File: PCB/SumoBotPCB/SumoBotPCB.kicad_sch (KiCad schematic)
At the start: 23 parts, among them M1 Motor_DC, M2 Motor_DC, M3 Motor_DC, M4 Motor_DC, SW1 SW_Push, U1 TB6612FNG, U10 VL53L0X-GY530, U11 VL53L0X-GY530, U12 VL53L0X-GY530, U2 hc-05_BLUETOOTH_MODULE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

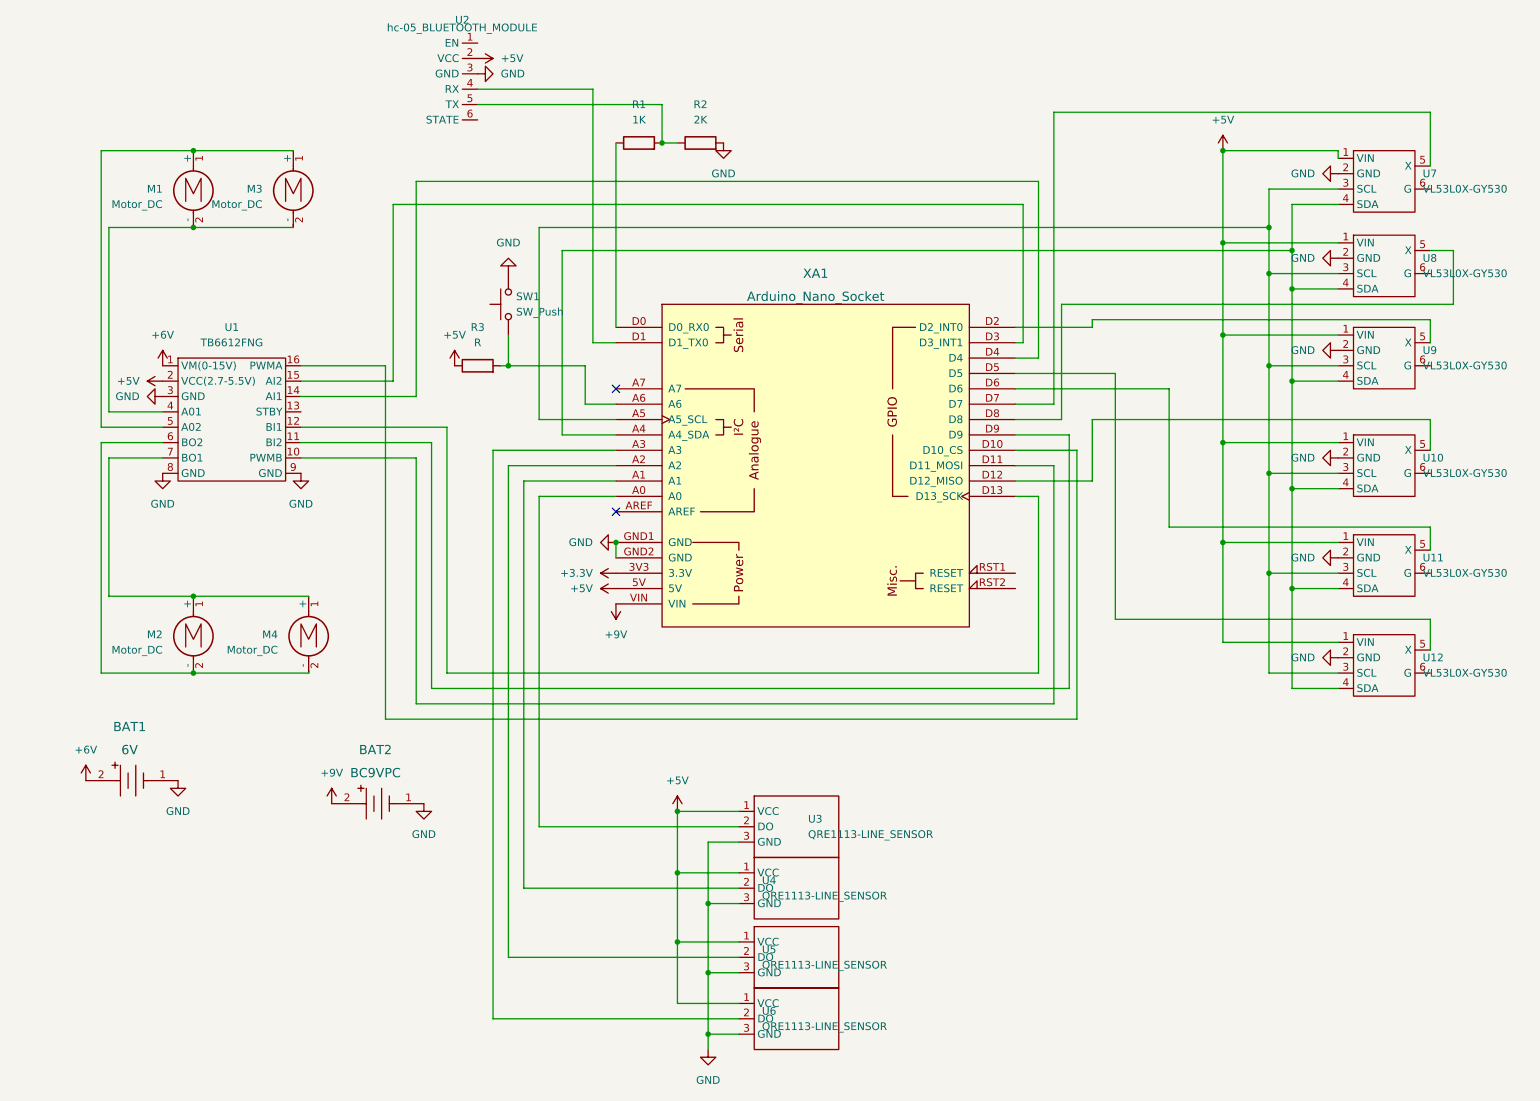
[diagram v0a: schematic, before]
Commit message: motor driver pwm
correct pin assignment to have motor driver use 6 pwm pins to allow all options.
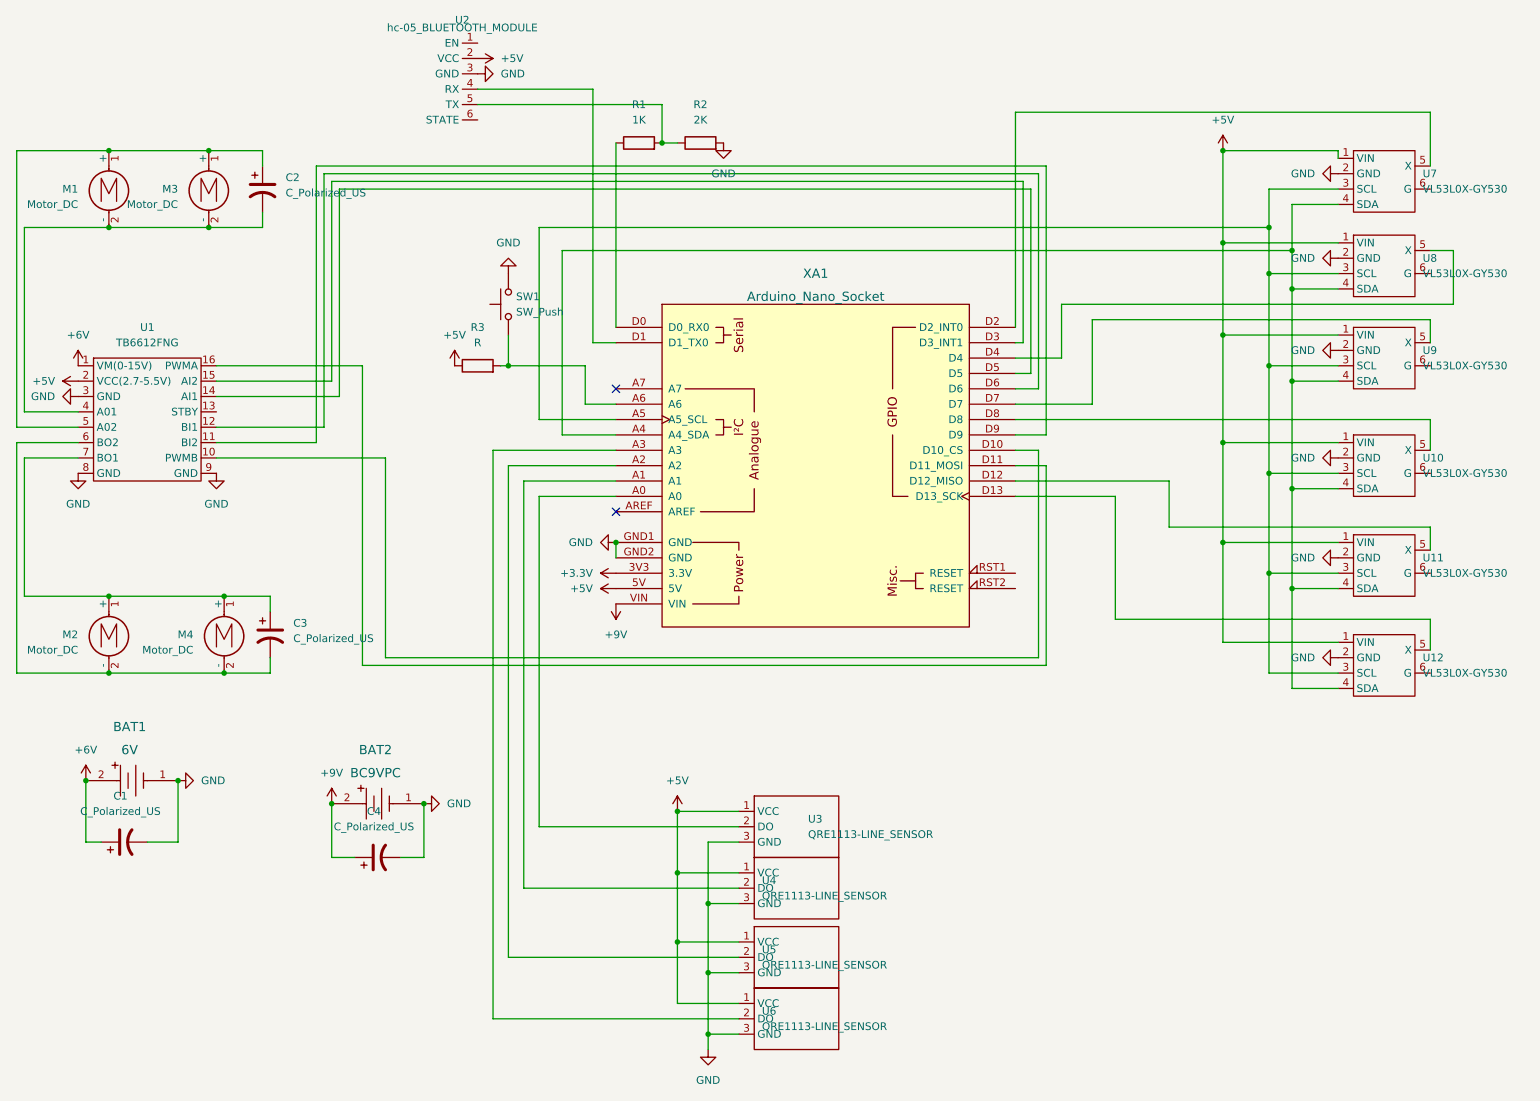
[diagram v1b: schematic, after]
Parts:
- added C1, C2, C3, C4: C_Polarized_US, Capacitor_THT:CP_Radial_D8.0mm_P5.00mm, symbol Device:C_Polarized_US
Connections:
- net +6V: now also C1.1
- net +9V: now also C4.1
- net GND: now also C1.2, C4.2
- net at M1.1 (+), M3.1 (+), U1.5 (A02): now also C2.1
- net at M1.2 (-), M3.2 (-), U1.4 (A01): now also C2.2
- net at U7.5 (X): now also XA1.D2 (D2_INT0); no longer XA1.D7
- net at M2.1 (+), M4.1 (+), U1.7 (BO1): now also C3.1
- net at M2.2 (-), M4.2 (-), U1.6 (BO2): now also C3.2
- net at U12.5 (X): now also XA1.D13 (D13_SCK); no longer XA1.D5
- net at U8.5 (X): now also XA1.D4; no longer XA1.D8
- net at U9.5 (X): now also XA1.D7; no longer XA1.D2 (D2_INT0)
- net at XA1.D10 (D10_CS): now also U1.10 (PWMB); no longer U1.16 (PWMA)
- net at XA1.D11 (D11_MOSI): now also U1.16 (PWMA); no longer U1.10 (PWMB)
- net at XA1.D12 (D12_MISO): now also U11.5 (X); no longer U10.5 (X)
- net at U1.12 (BI1): now also XA1.D6; no longer XA1.D13 (D13_SCK)
- net at U1.14 (AI1): now also XA1.D5; no longer XA1.D4
- new net: U10.5 (X), XA1.D8
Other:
- moved on the sheet: M1, M2, M3, M4, U1

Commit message: ADDED STANDBY SWITCH
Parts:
- added SW2: SW_SPDT, custom:SpDt SlideSwitch, symbol Switch:SW_SPDT
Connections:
- net +5V: now also SW2.1 (A)
- net at U1.13 (STBY): now also SW2.2 (B)
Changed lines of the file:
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@@
+    (stroke (width 0) (type default) (color 0 0 0 0))
+  )
+  (wire (pts (xy 54.61 64.77) (xy 54.61 53.34))
     (stroke (width 0) (type default) (color 0 0 0 0))
   )
@@
   )
   (wire (pts (xy 30.48 107.95) (xy 15.24 107.95))
+    (stroke (width 0) (type default) (color 0 0 0 0))
+  )
+  (wire (pts (xy 48.26 64.77) (xy 54.61 64.77))
     (stroke (width 0) (type default) (color 0 0 0 0))
   )
@@
     )
     (property "Datasheet" "" (id 3) (at 25.4 57.15 0)
+      (effects (font (size 1.27 1.27)) hide)
+    )
+    (pin "1")
+  )
+  (symbol (lib_id "power:+5V") (at 52.07 43.18 0) (unit 1)
+    (in_bom yes) (on_board yes) (fields_autoplaced)
+    (property "Reference" "#PWR0128" (id 0) (at 52.07 46.99 0)
+      (effects (font (size 1.27 1.27)) hide)
+    )
+    (property "Value" "+5V" (id 1) (at 52.07 38.1 0))
+    (property "Footprint" "" (id 2) (at 52.07 43.18 0)
+      (effects (font (size 1.27 1.27)) hide)
+    )
+    (property "Datasheet" "" (id 3) (at 52.07 43.18 0)
       (effects (font (size 1.27 1.27)) hide)
     )
@@
     (pin "1")
   )
+  (symbol (lib_id "Switch:SW_SPDT") (at 54.61 48.26 90) (unit 1)
+    (in_bom yes) (on_board yes) (fields_autoplaced)
+    (property "Reference" "SW2" (id 0) (at 58.42 46.9899 90)
+      (effects (font (size 1.27 1.27)) (justify right))
+    )
+    (property "Value" "SW_SPDT" (id 1) (at 58.42 49.5299 90)
+      (effects (font (size 1.27 1.27)) (justify right))
+    )
+    (property "Footprint" "custom:SpDt SlideSwitch" (id 2) (at 54.61 48.26 0)
+      (effects (font (size 1.27 1.27)) hide)
+    )
+    (property "Datasheet" "~" (id 3) (at 54.61 48.26 0)
+      (effects (font (size 1.27 1.27)) hide)
+    )
+    (pin "1")
+    (pin "2")
+    (pin "3")
+  )
   (symbol (lib_id "Switch:SW_Push") (at 96.52 46.99 90) (unit 1)
     (in_bom yes) (on_board yes) (fields_autoplaced)
@@
       (reference "#PWR0127") (unit 1) (value "GND") (footprint "")
     )
+    (path "/58827ba0-4d07-44f4-b07b-8842098ca099"
+      (reference "#PWR0128") (unit 1) (value "+5V") (footprint "")
+    )
     (path "/c13e6644-1617-41c6-92ae-d1ca64618352"
       (reference "BAT1") (unit 1) (value "6V") (footprint "Connector_PinHeader_2.54mm:PinHeader_1x02_P2.54mm_Vertical")
@@
       (reference "SW1") (unit 1) (value "SW_Push") (footprint "Button_Switch_THT:SW_PUSH_6mm_H4.3mm")
     )
+    (path "/b01b6e50-2c09-4c1a-87df-69dce96dfaa6"
+      (reference "SW2") (unit 1) (value "SW_SPDT") (footprint "custom:SpDt SlideSwitch")
+    )
     (path "/f86527b4-a225-4f07-a789-d53d38094b3b"

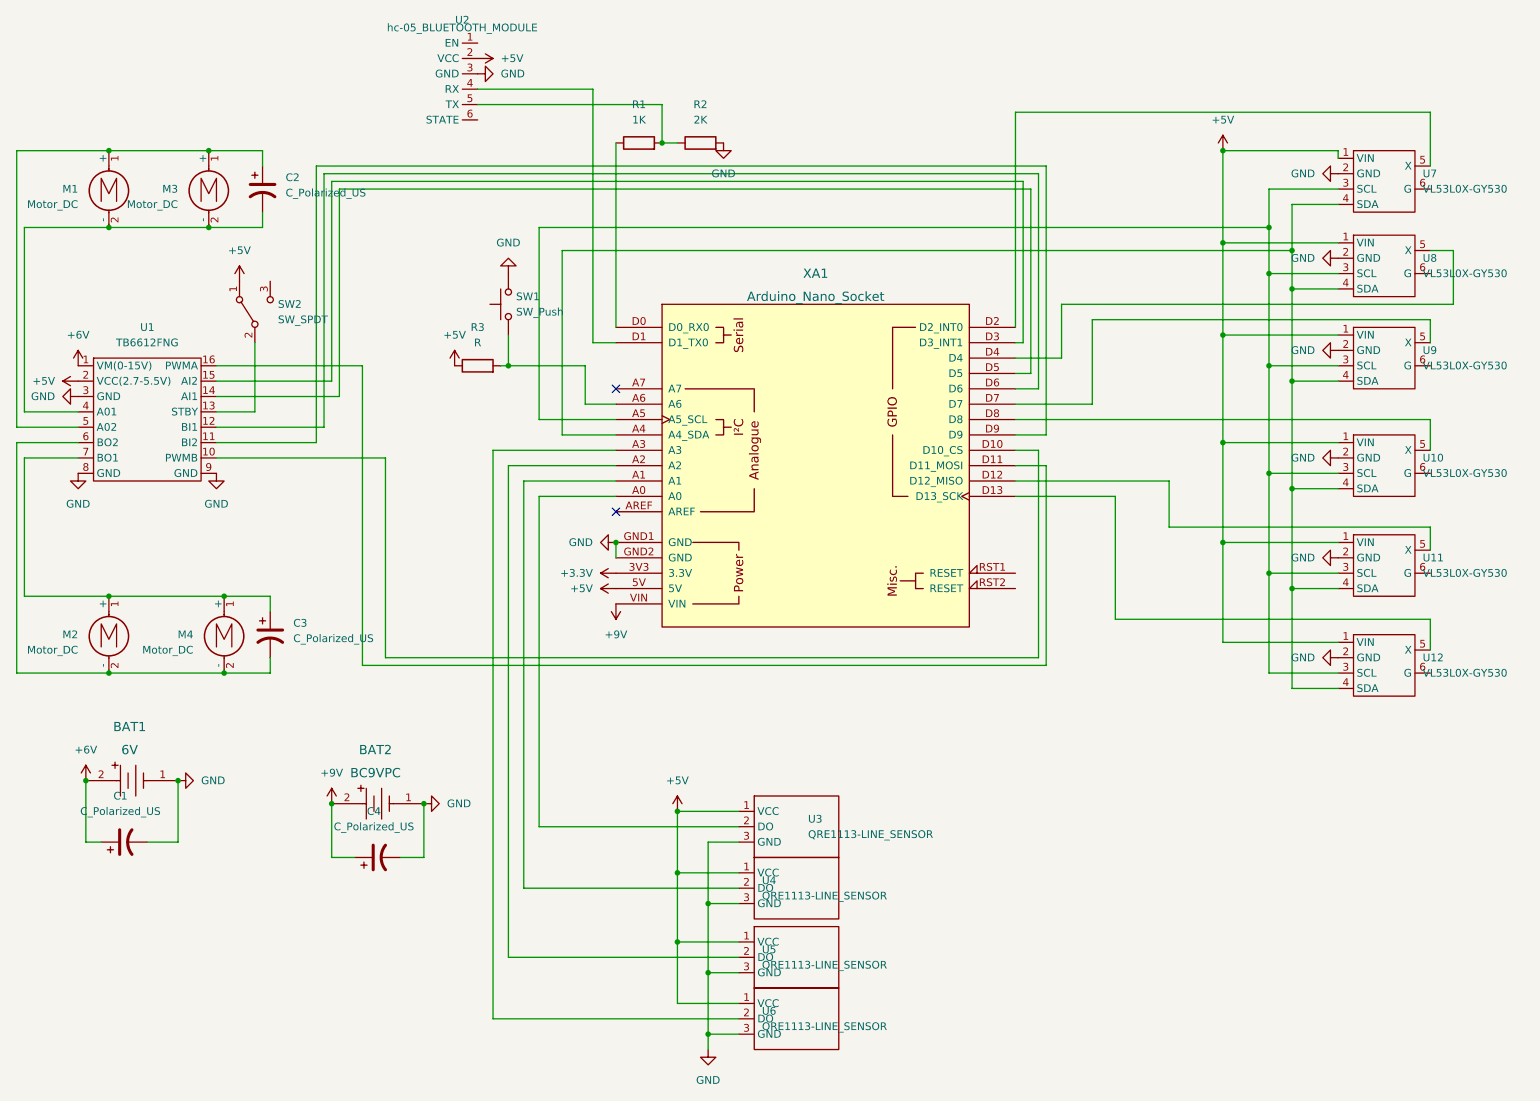
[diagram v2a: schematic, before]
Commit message: re-assigned pins
changed pin assignments on analog pins
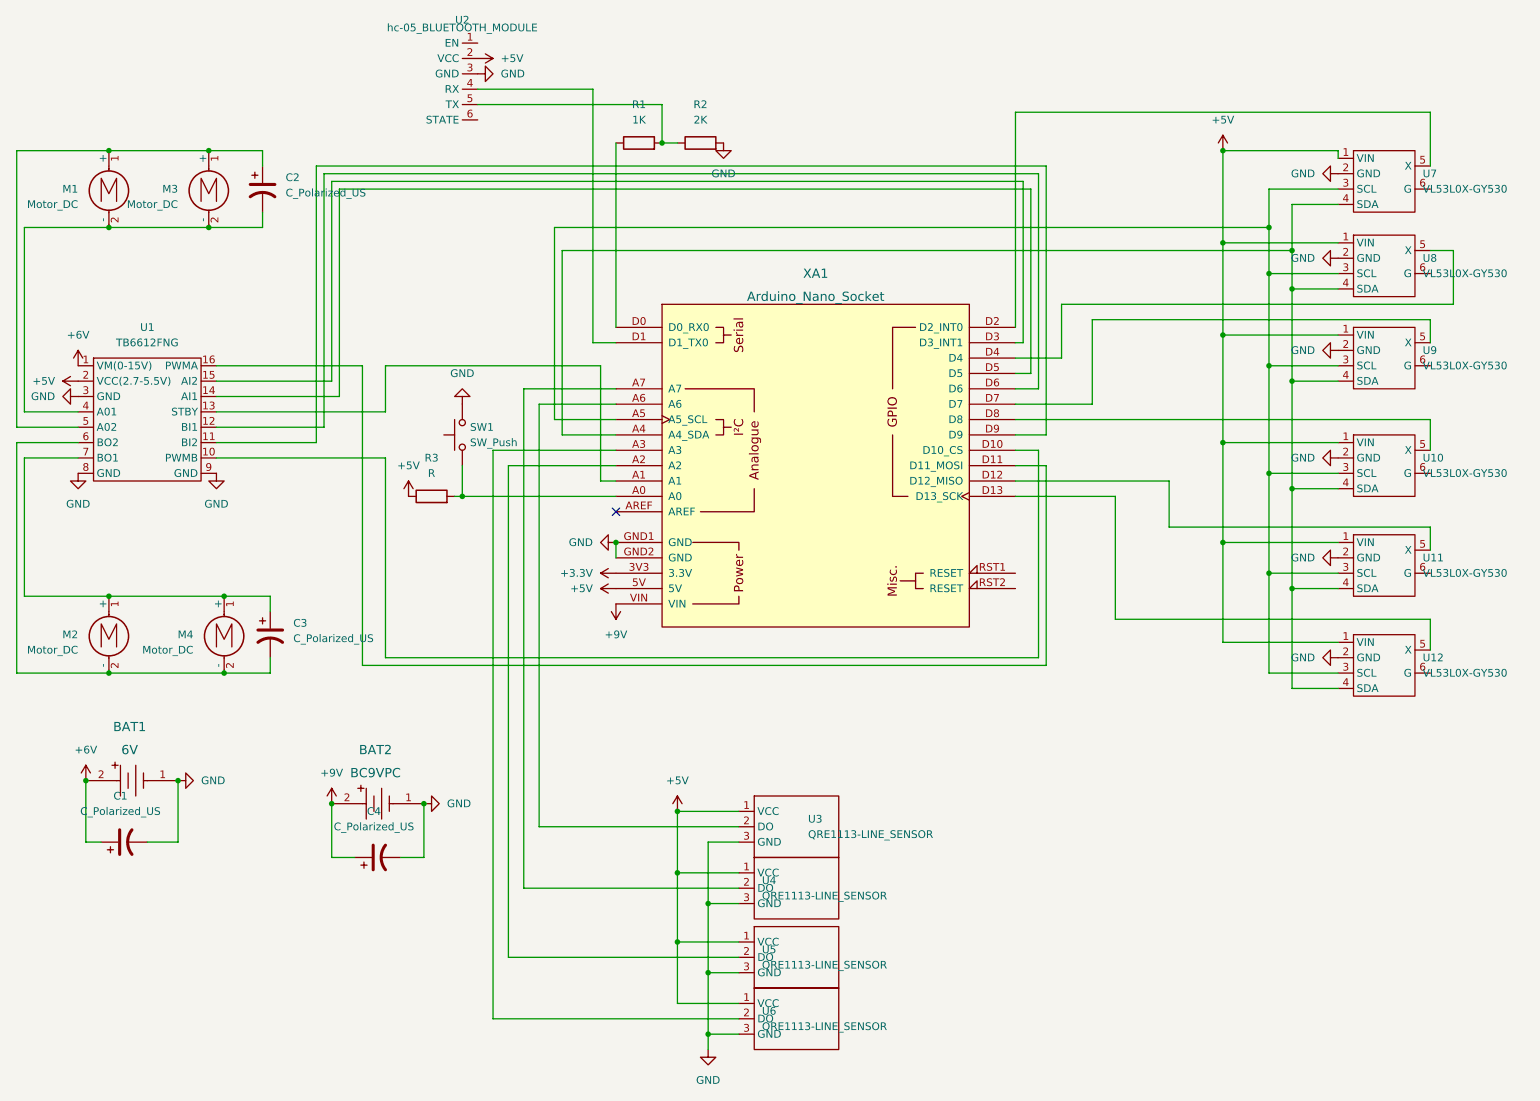
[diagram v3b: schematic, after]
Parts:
- removed SW2: SW_SPDT, custom:SpDt SlideSwitch, symbol Switch:SW_SPDT
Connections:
- net at U3.2 (DO): now also XA1.A6; no longer XA1.A0
- net at R3.2, SW1.1: now also XA1.A0; no longer XA1.A6
- net at XA1.A1: now also U1.13 (STBY); no longer U4.2 (DO)
- net at XA1.A7: now also U4.2 (DO)
- no-connect marks 2 -> 1
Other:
- moved on the sheet: R3, SW1

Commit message: cleaned up schematic
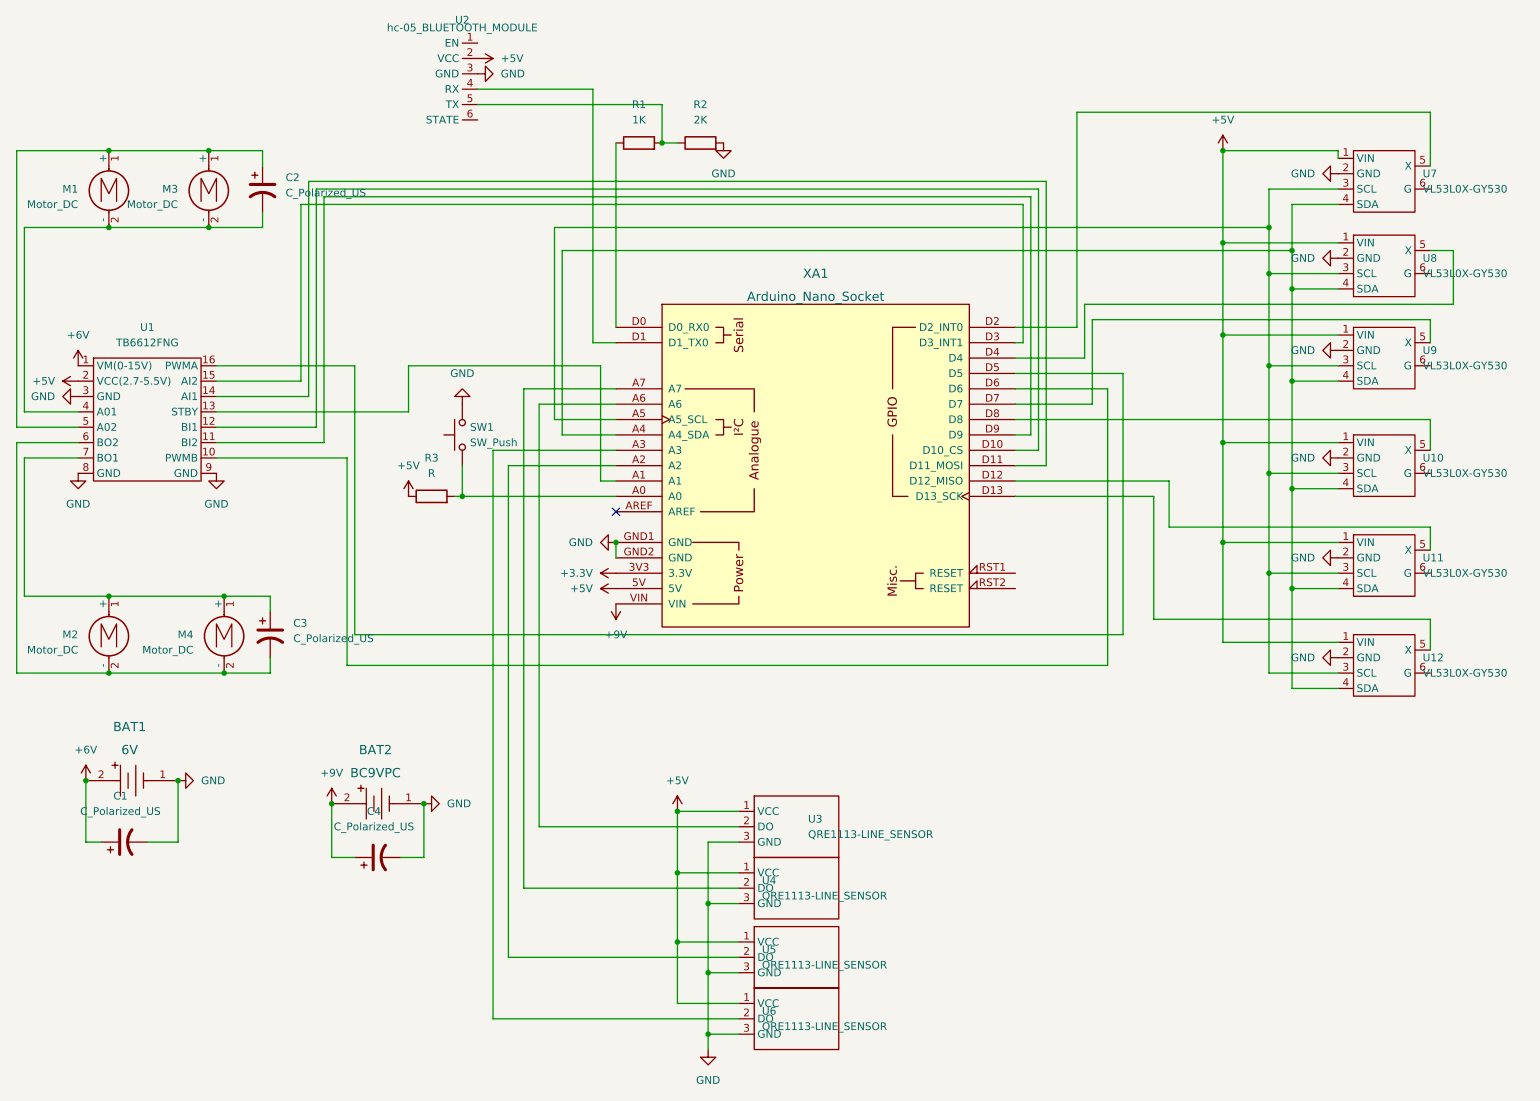
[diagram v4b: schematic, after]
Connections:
- net at XA1.D10 (D10_CS): now also U1.12 (BI1); no longer U1.10 (PWMB)
- net at XA1.D11 (D11_MOSI): now also U1.14 (AI1); no longer U1.16 (PWMA)
- net at XA1.D5: now also U1.16 (PWMA); no longer U1.14 (AI1)
- net at XA1.D6: now also U1.10 (PWMB); no longer U1.12 (BI1)
